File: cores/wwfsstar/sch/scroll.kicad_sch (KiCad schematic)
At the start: 13 parts, among them IC100 74LS194, IC101 74LS158, IC112 24J6-0, IC113 24J7-0, IC79 74LS157, IC80 74LS157, IC81 74LS273, IC82 74LS273, IC83 74LS273, IC84 74LS273, IC97 74LS194, IC98 74LS194, IC99 74LS194

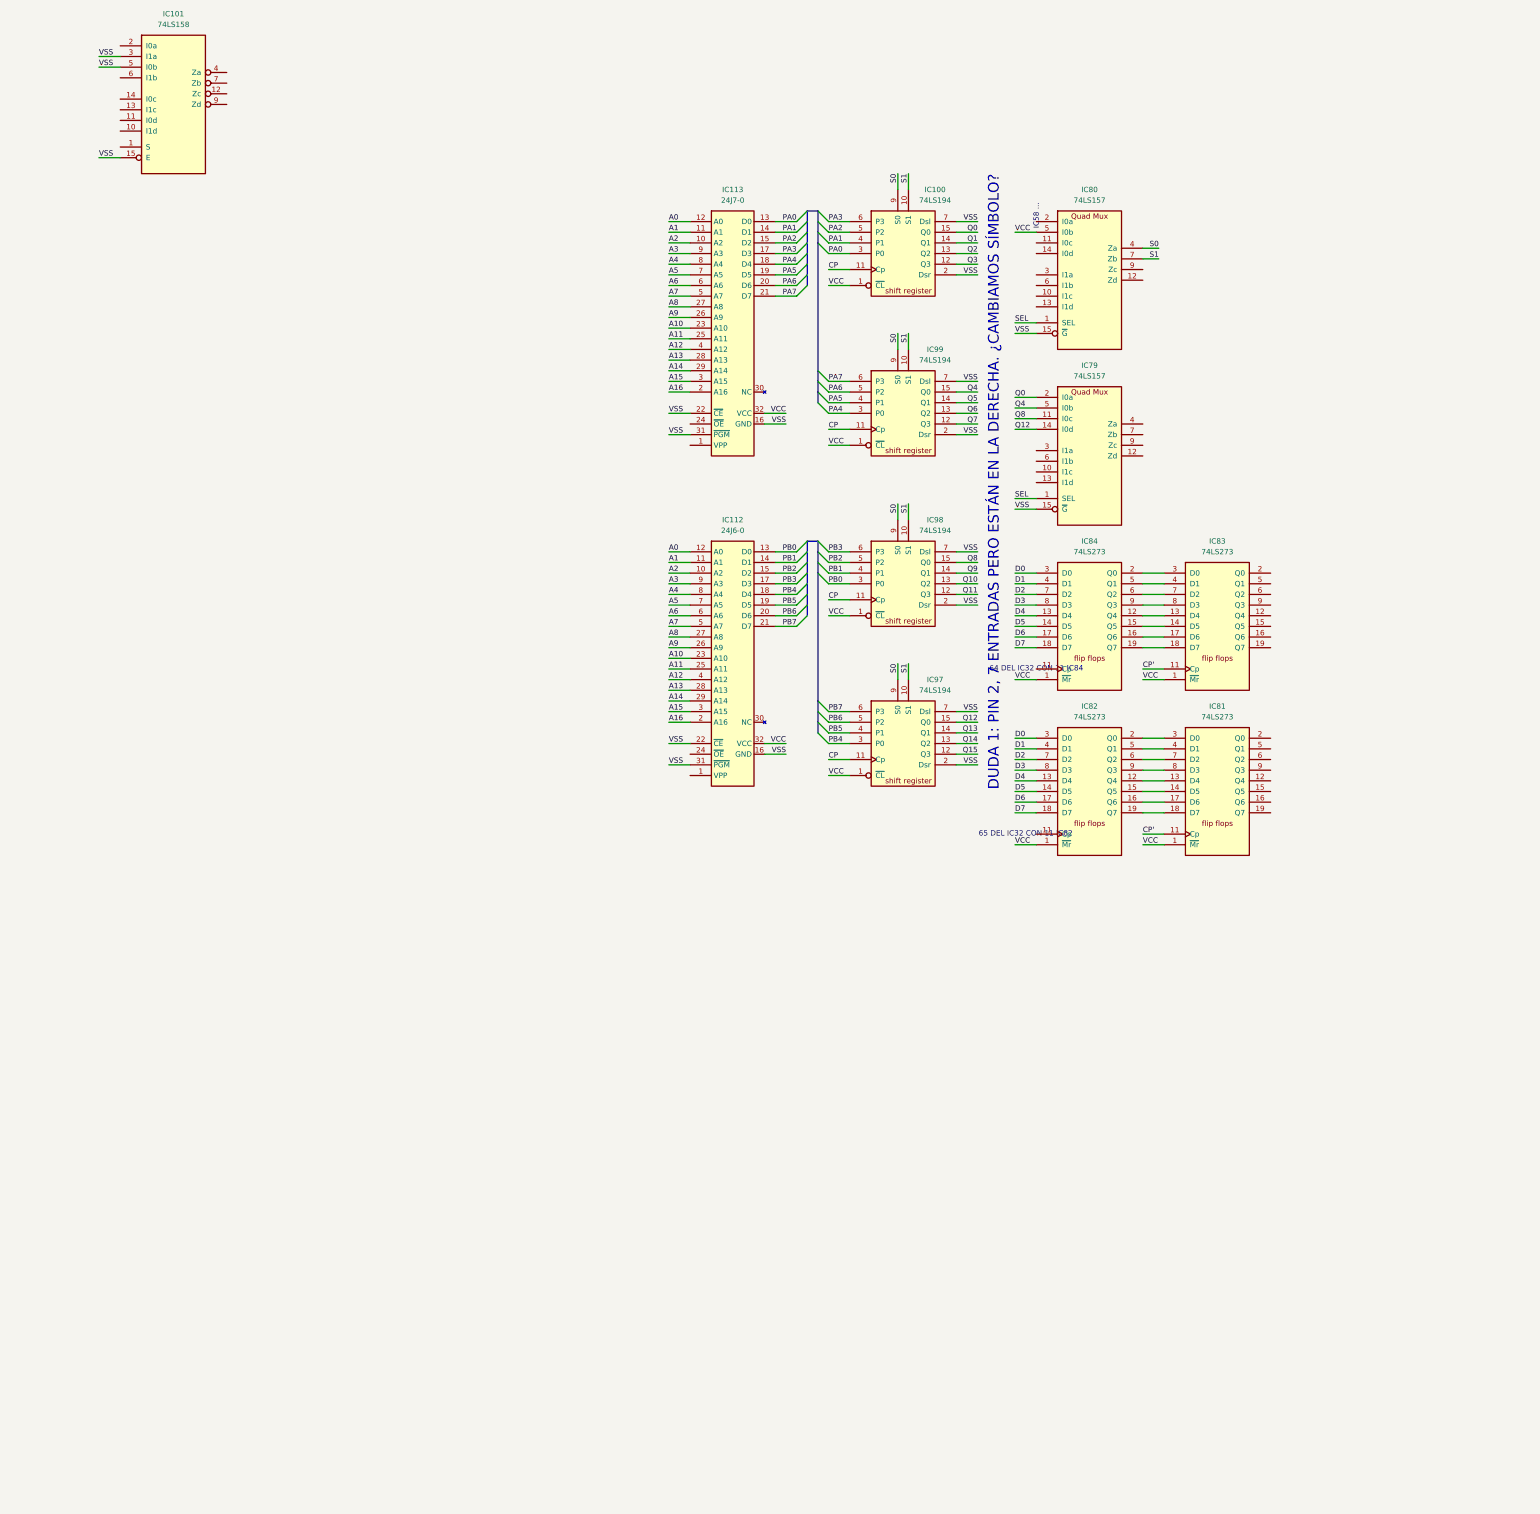
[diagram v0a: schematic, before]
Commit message: wwfsstar sch: working on scroll page
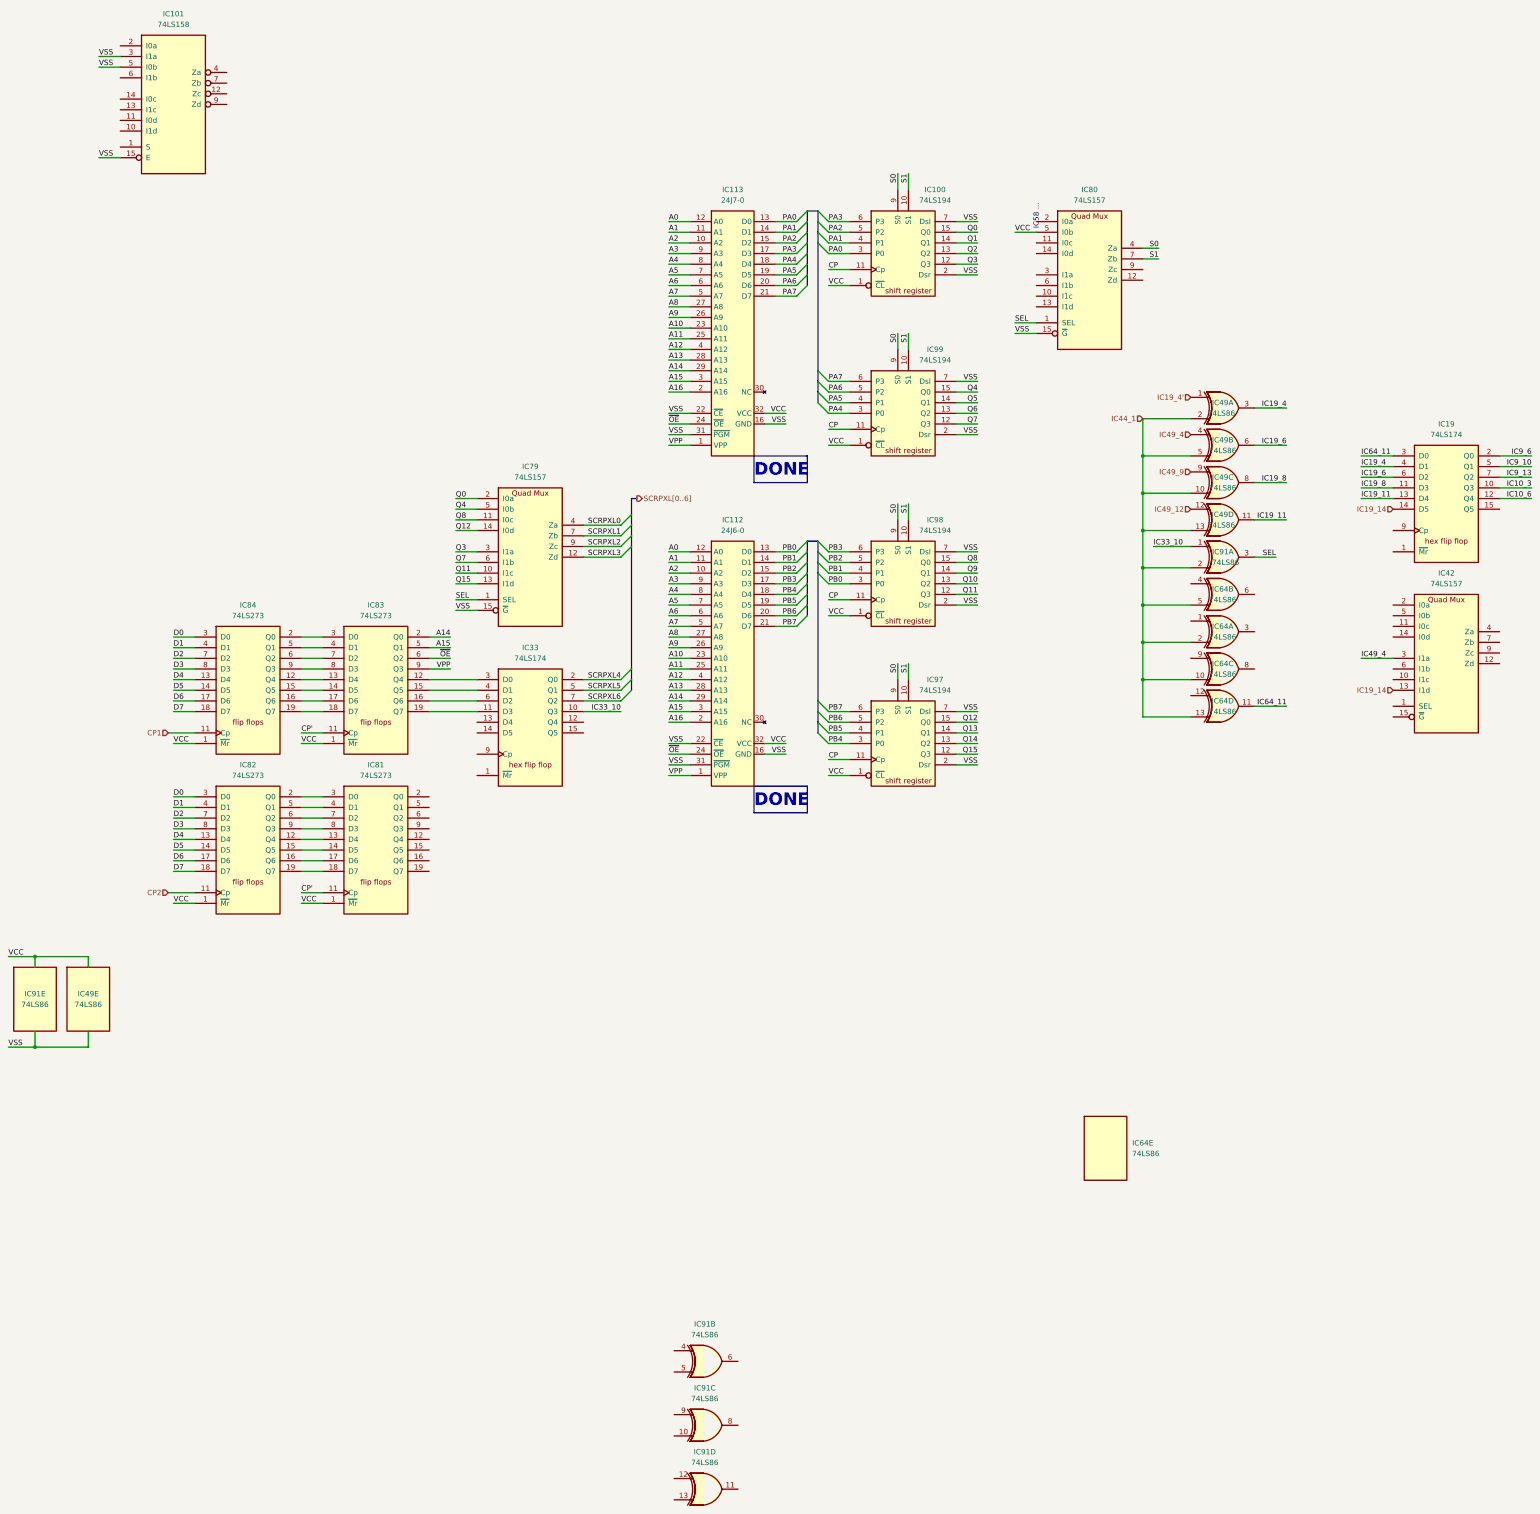
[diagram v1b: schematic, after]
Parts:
- added IC19, IC33: 74LS174, symbol jt74:74LS174
- added IC42: 74LS157, symbol jt74:74LS157
- added IC49, IC64, IC91: 74LS86, symbol jt74:74LS86
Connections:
- net A14: now also IC83.2 (Q0)
- net A15: now also IC83.5 (Q1)
- net Q11: now also IC79.10 (I1c)
- net Q15: now also IC79.13 (I1d)
- net Q3: now also IC79.3 (I1a)
- net Q7: now also IC79.6 (I1b)
- net SEL: now also IC91.3
- net VCC: now also IC19.16 (VCC), IC33.16 (VCC), IC49.14 (VCC), IC64.14 (VCC), IC91.14 (VCC)
- net VSS: now also IC19.8 (VSS), IC33.8 (VSS), IC49.7 (VSS), IC64.7 (VSS), IC91.7 (VSS)
- net VPP: now reaches IC112.1 (VPP)
- net VPP: now also IC113.1 (VPP), IC83.9 (Q3)
- net ~{OE}: now reaches IC112.24 (~{OE})
- net ~{OE}: now also IC113.24 (~{OE}), IC83.6 (Q2)
- net at IC83.12 (Q4): now also IC33.3 (D0)
- net at IC83.15 (Q5): now also IC33.4 (D1)
- net at IC83.16 (Q6): now also IC33.6 (D2)
- net at IC83.19 (Q7): now also IC33.11 (D3)
- net CP1: now reaches IC84.11 (Cp)
- net SCRPXL3: now reaches IC79.12 (Zd)
- net SCRPXL0: now reaches IC79.4 (Za)
- net SCRPXL1: now reaches IC79.7 (Zb)
- net SCRPXL2: now reaches IC79.9 (Zc)
- net CP2: now reaches IC82.11 (Cp)
- new net IC10_3: IC19.10 (Q3)
- new net IC10_6: IC19.12 (Q4)
- new net IC19_11: IC19.13 (D4), IC49.11
- new net IC19_14: IC19.14 (D5), IC42.13 (I1d)
- new net IC19_4: IC19.4 (D1), IC49.3
- new net IC19_4': IC49.1
- new net IC19_6: IC19.6 (D2), IC49.6
- new net IC19_8: IC19.11 (D3), IC49.8
- new net IC33_10: IC33.10 (Q3), IC91.1
- new net IC44_1: IC49.10, IC49.13, IC49.2, IC49.5, IC64.10, IC64.13, IC64.2, IC64.5, IC91.2
- new net IC49_12: IC49.12
- new net IC49_4: IC42.3 (I1a), IC49.4
- new net IC49_9: IC49.9
- new net IC64_11: IC19.3 (D0), IC64.11
- new net IC9_10: IC19.5 (Q1)
- new net IC9_13: IC19.7 (Q2)
- new net IC9_6: IC19.2 (Q0)
- new net SCRPXL4: IC33.2 (Q0)
- new net SCRPXL5: IC33.5 (Q1)
- new net SCRPXL6: IC33.7 (Q2)
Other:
- note added: "DONE"
- note removed: "64 DEL IC32 CON 11 IC84"
- note removed: "65 DEL IC32 CON 11 IC82"
- note removed: "DUDA 1: PIN 2, 7 ENTRADAS PERO ESTÁN EN LA DERECHA. ¿CAMBIAMOS SÍMBOLO?"
- moved on the sheet: IC79, IC81, IC82, IC83, IC84

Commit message: wwfsstar: io edits
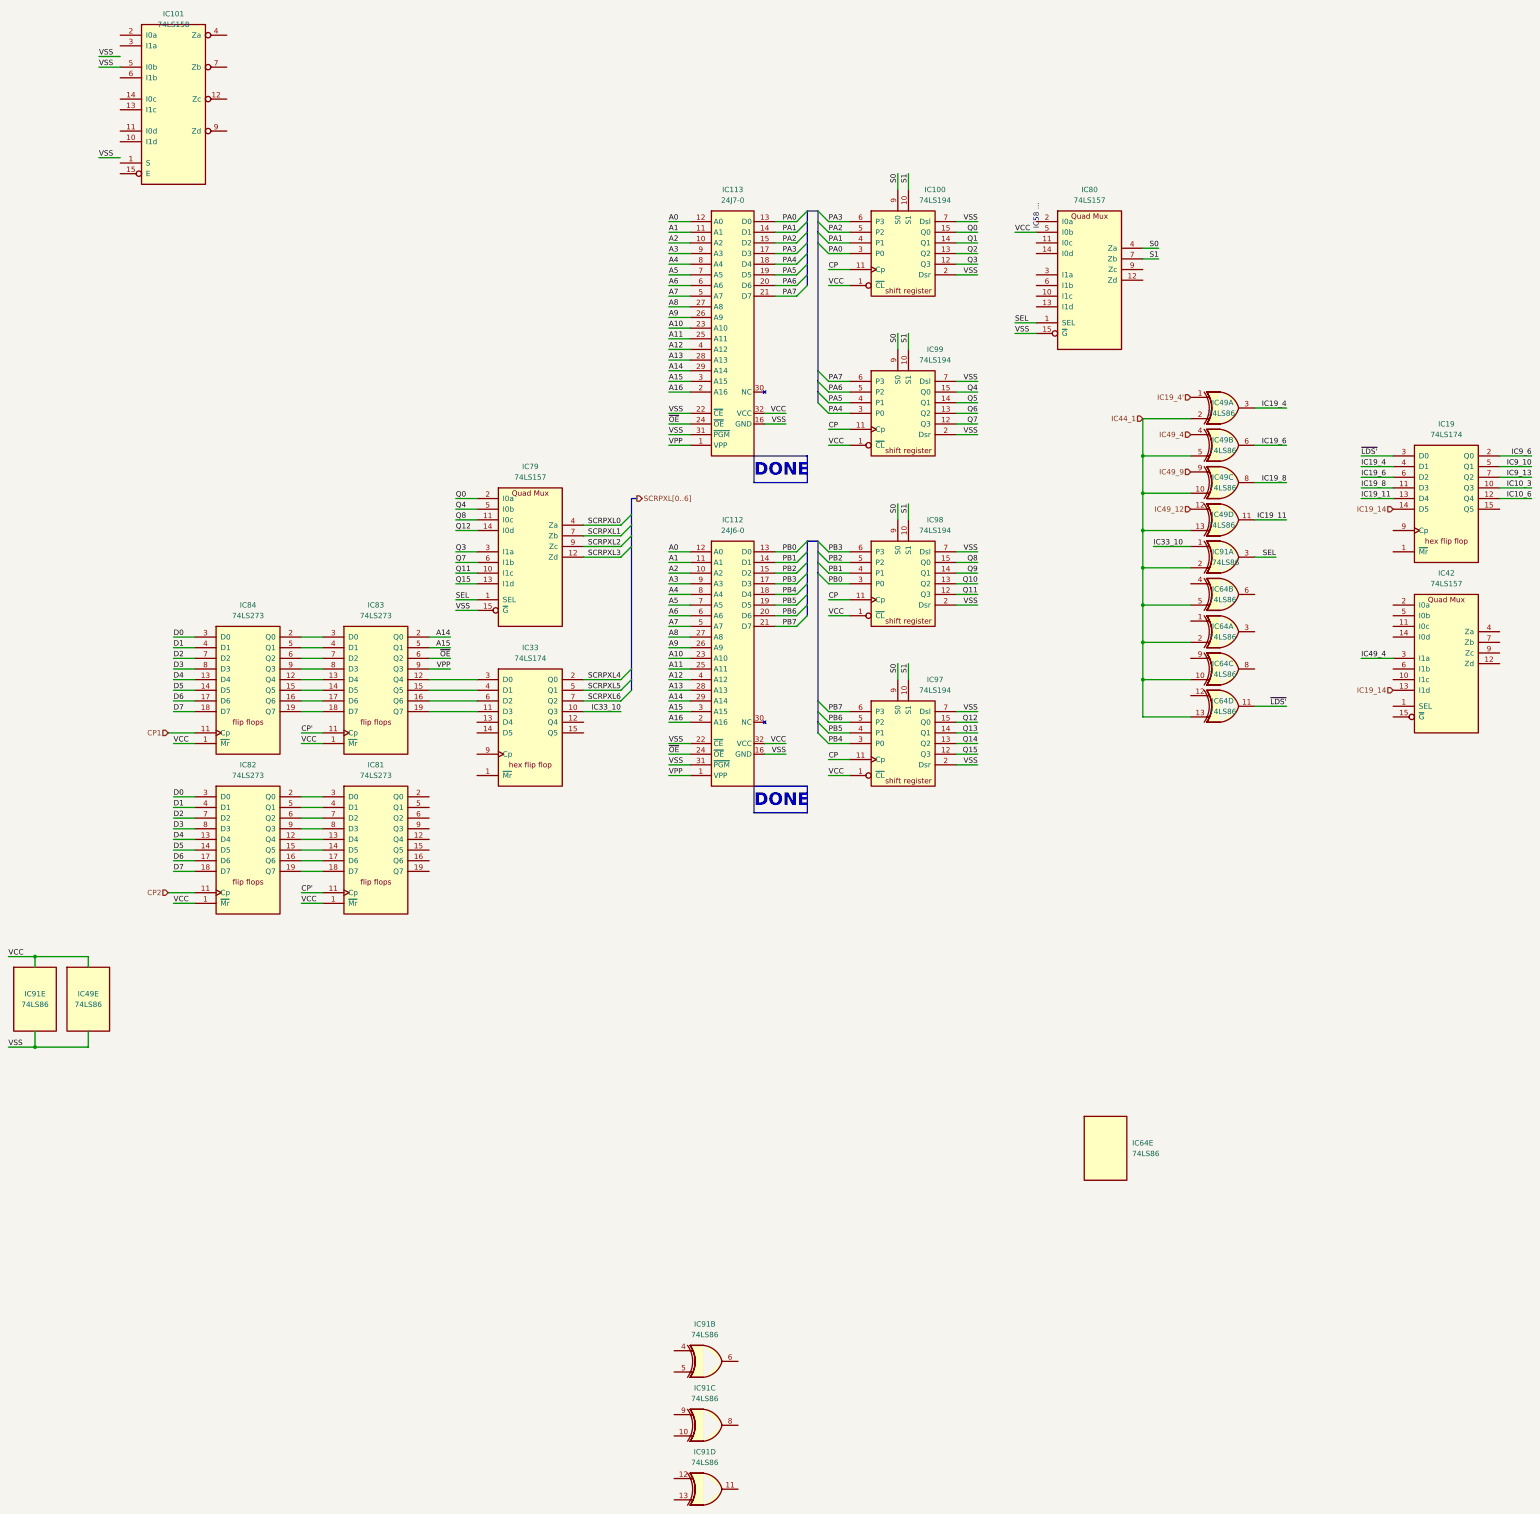
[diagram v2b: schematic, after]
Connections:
- net VSS: no longer IC101.15 (E), IC101.3 (I1a)
- net IC64_11 renamed ~{LDS'}
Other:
- company: (none) -> JOTEGO
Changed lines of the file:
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@@
 	(generator_version "8.0")
 	(paper "A3")
+	(title_block
+		(company "JOTEGO")
+	)
 	(junction
 		(at 19.05 261.62)
@@
 		)
 	)
-	(label "IC64_11"
+	(label "~{LDS'}"
 		(at 335.28 142.24 0)
 		(fields_autoplaced yes)
@@
 		)
 	)
-	(label "IC64_11"
+	(label "~{LDS'}"
 		(at 317.5 201.93 180)
 		(fields_autoplaced yes)
@@
 	)
 	(symbol
-		(lib_name "74LS273_3")
 		(lib_id "jt74:74LS273")
 		(at 69.85 198.12 0)
@@
 	)
 	(symbol
-		(lib_name "74LS273_2")
 		(lib_id "jt74:74LS273")
 		(at 69.85 236.22 0)
@@
 	)
 	(symbol
-		(lib_name "74LS273_1")
 		(lib_id "jt74:74LS273")
 		(at 100.33 236.22 0)

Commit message: wwfsstar: sch -- video memory on bottom board
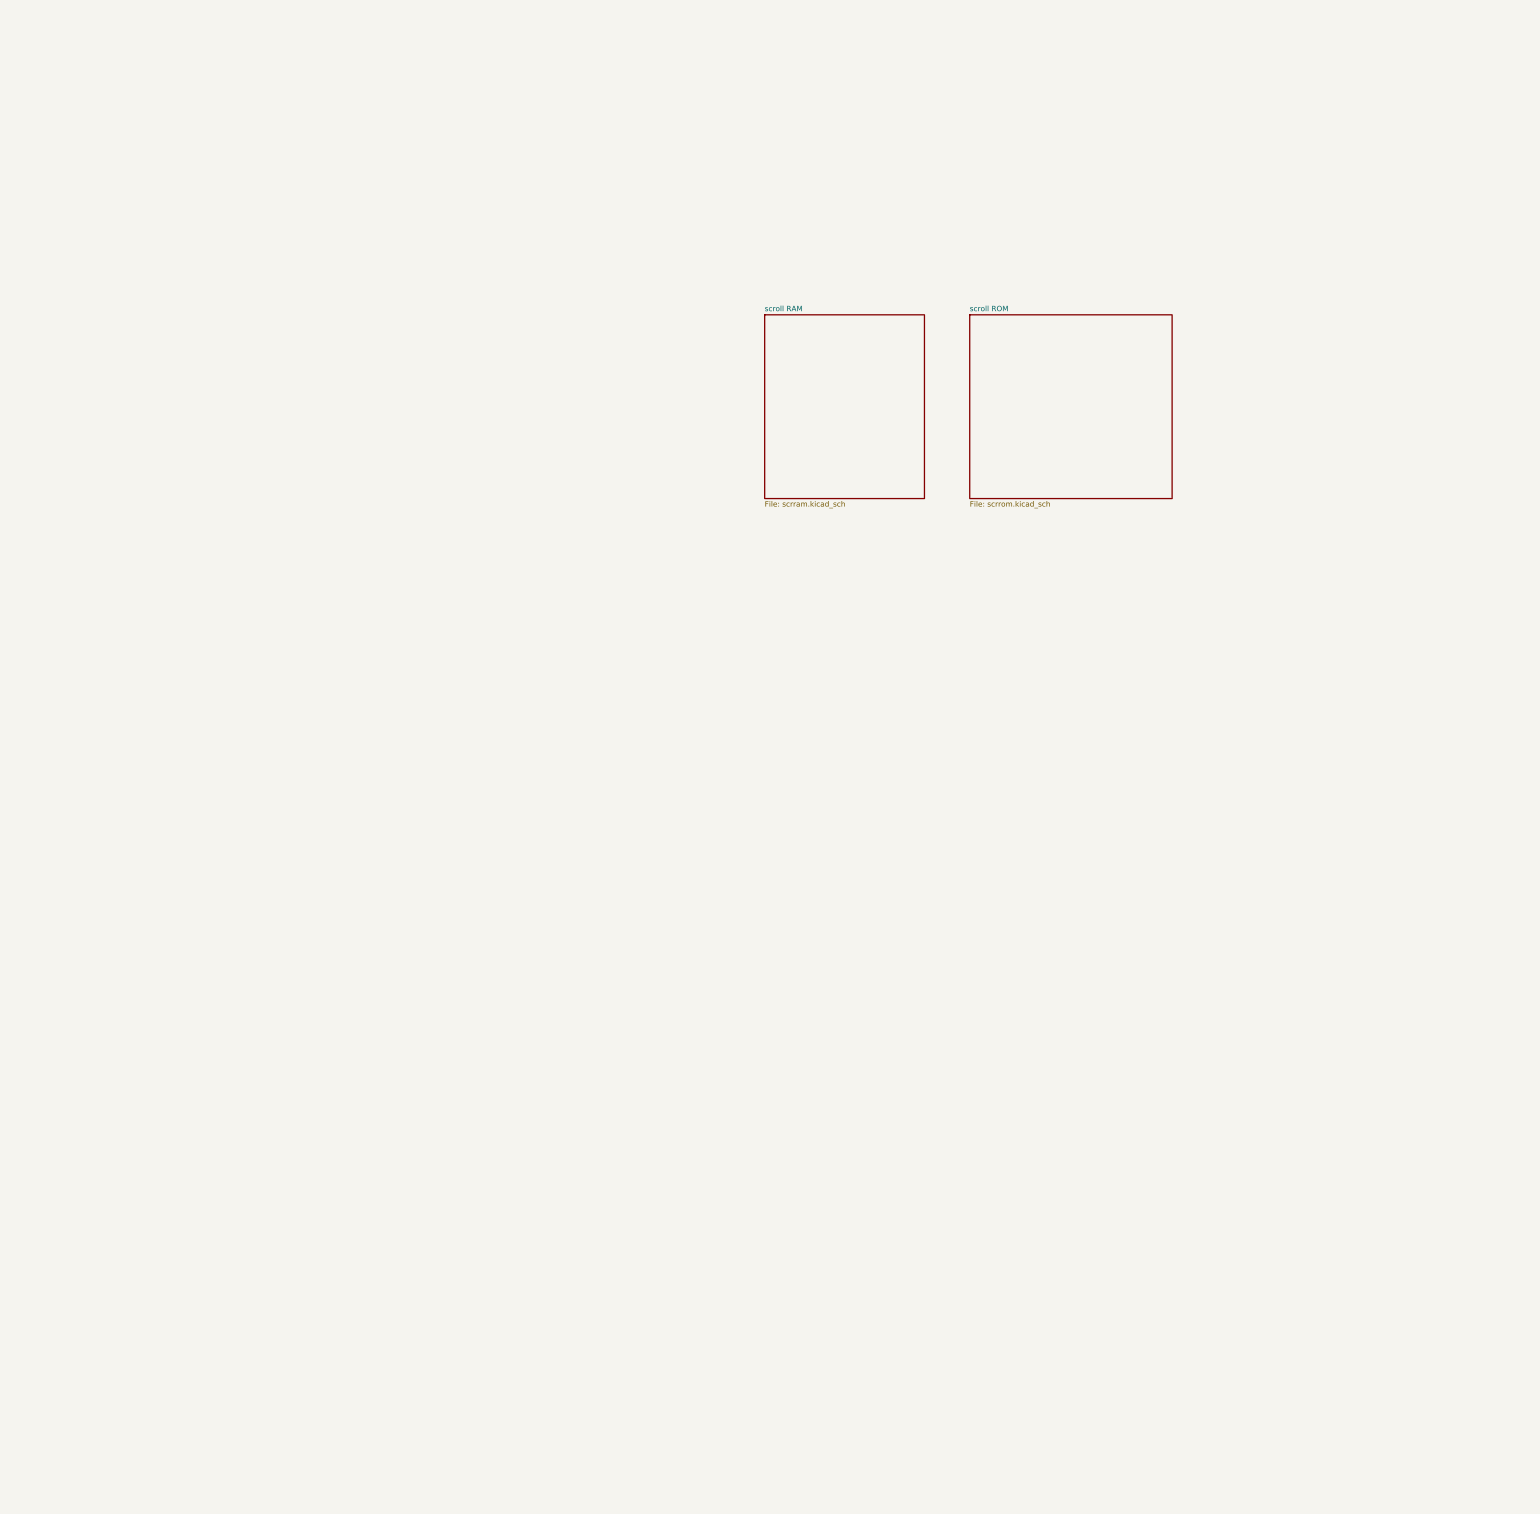
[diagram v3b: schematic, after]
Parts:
- removed IC100, IC97, IC98, IC99: 74LS194, symbol jt74:74LS194
- removed IC101: 74LS158, symbol jt74:74LS158
- removed IC112: 24J6-0, symbol jt_rom:27C1000
- removed IC113: 24J7-0, symbol jt_rom:27C1000
- removed IC19, IC33: 74LS174, symbol jt74:74LS174
- removed IC42, IC79, IC80: 74LS157, symbol jt74:74LS157
- removed IC49, IC64, IC91: 74LS86, symbol jt74:74LS86
- removed IC81, IC82, IC83, IC84: 74LS273, symbol jt74:74LS273
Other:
- added sheet scroll RAM (scrram.kicad_sch)
- added sheet scroll ROM (scrrom.kicad_sch)
- note removed: "DONE"
- note removed: "IC58 ..."
